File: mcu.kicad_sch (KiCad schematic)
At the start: 41 parts, among them U1 STM32U5G9ZJTxQ, Y1 NX2016SA-16MHZ-EXS00A-CS07826, Y2 NX2012SA-32.768K-STD-MUB-1

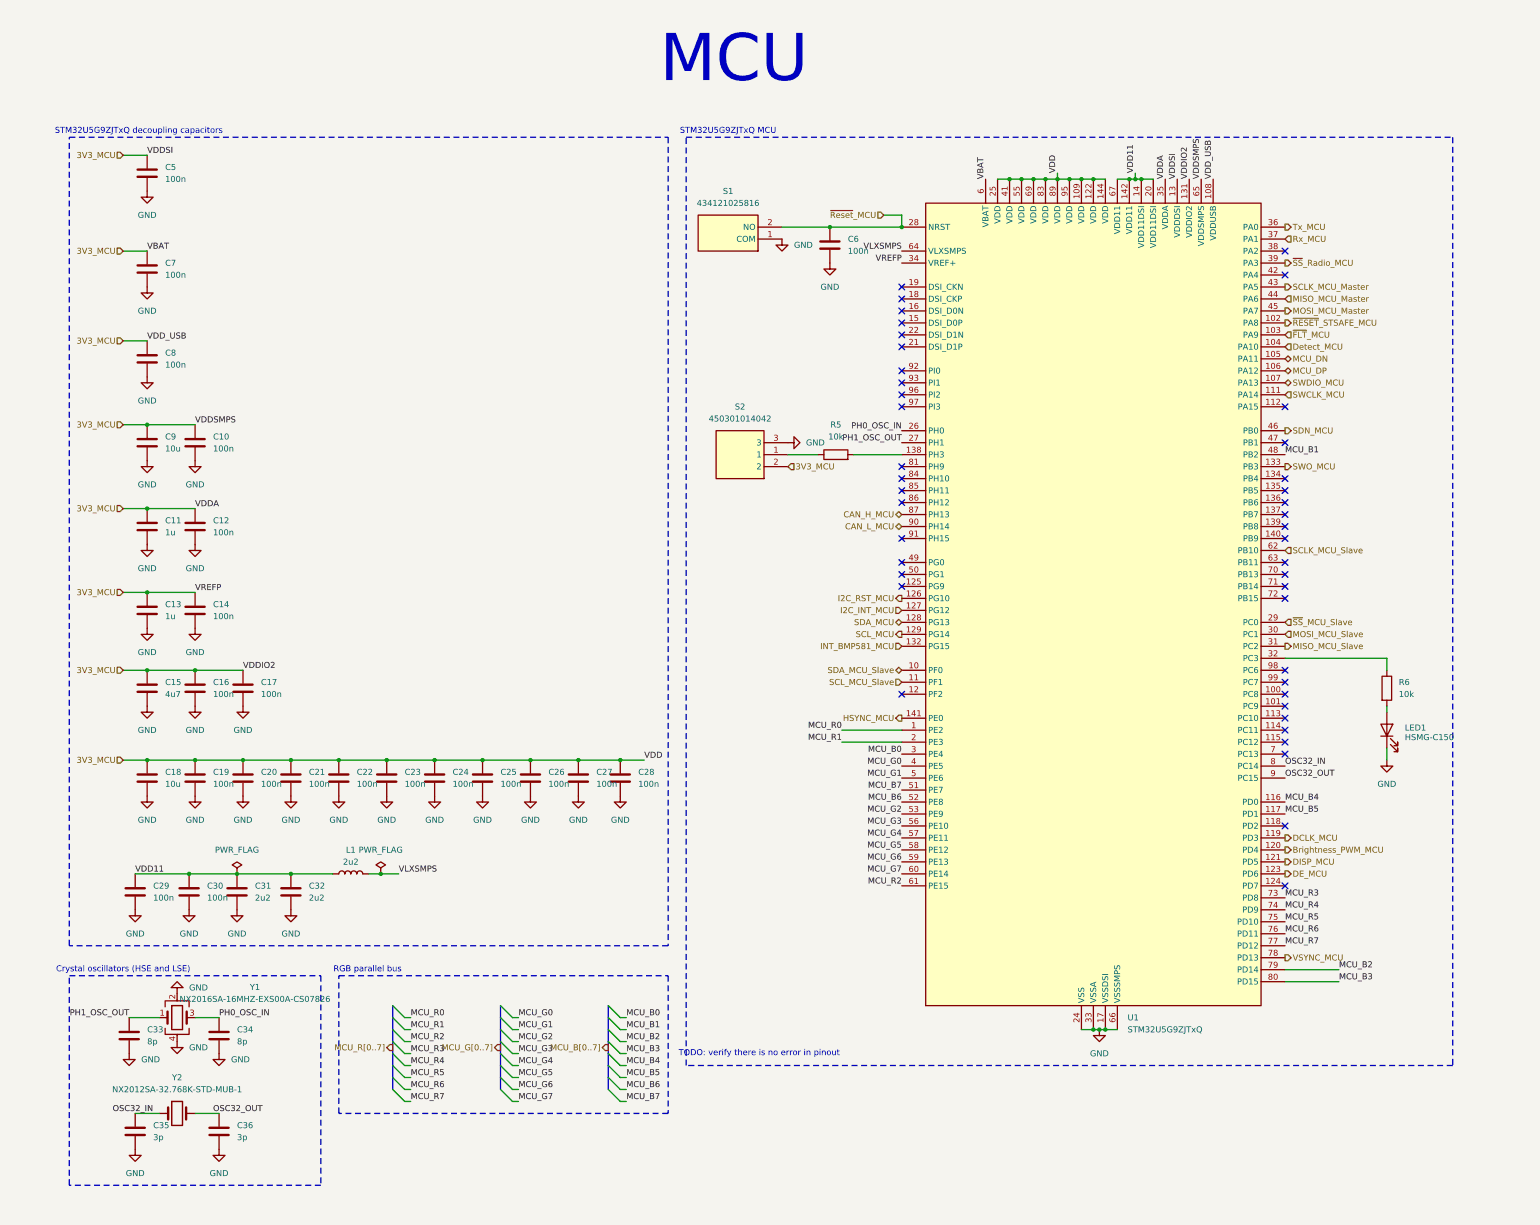
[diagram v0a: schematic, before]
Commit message: Update schematic to Kicad 10
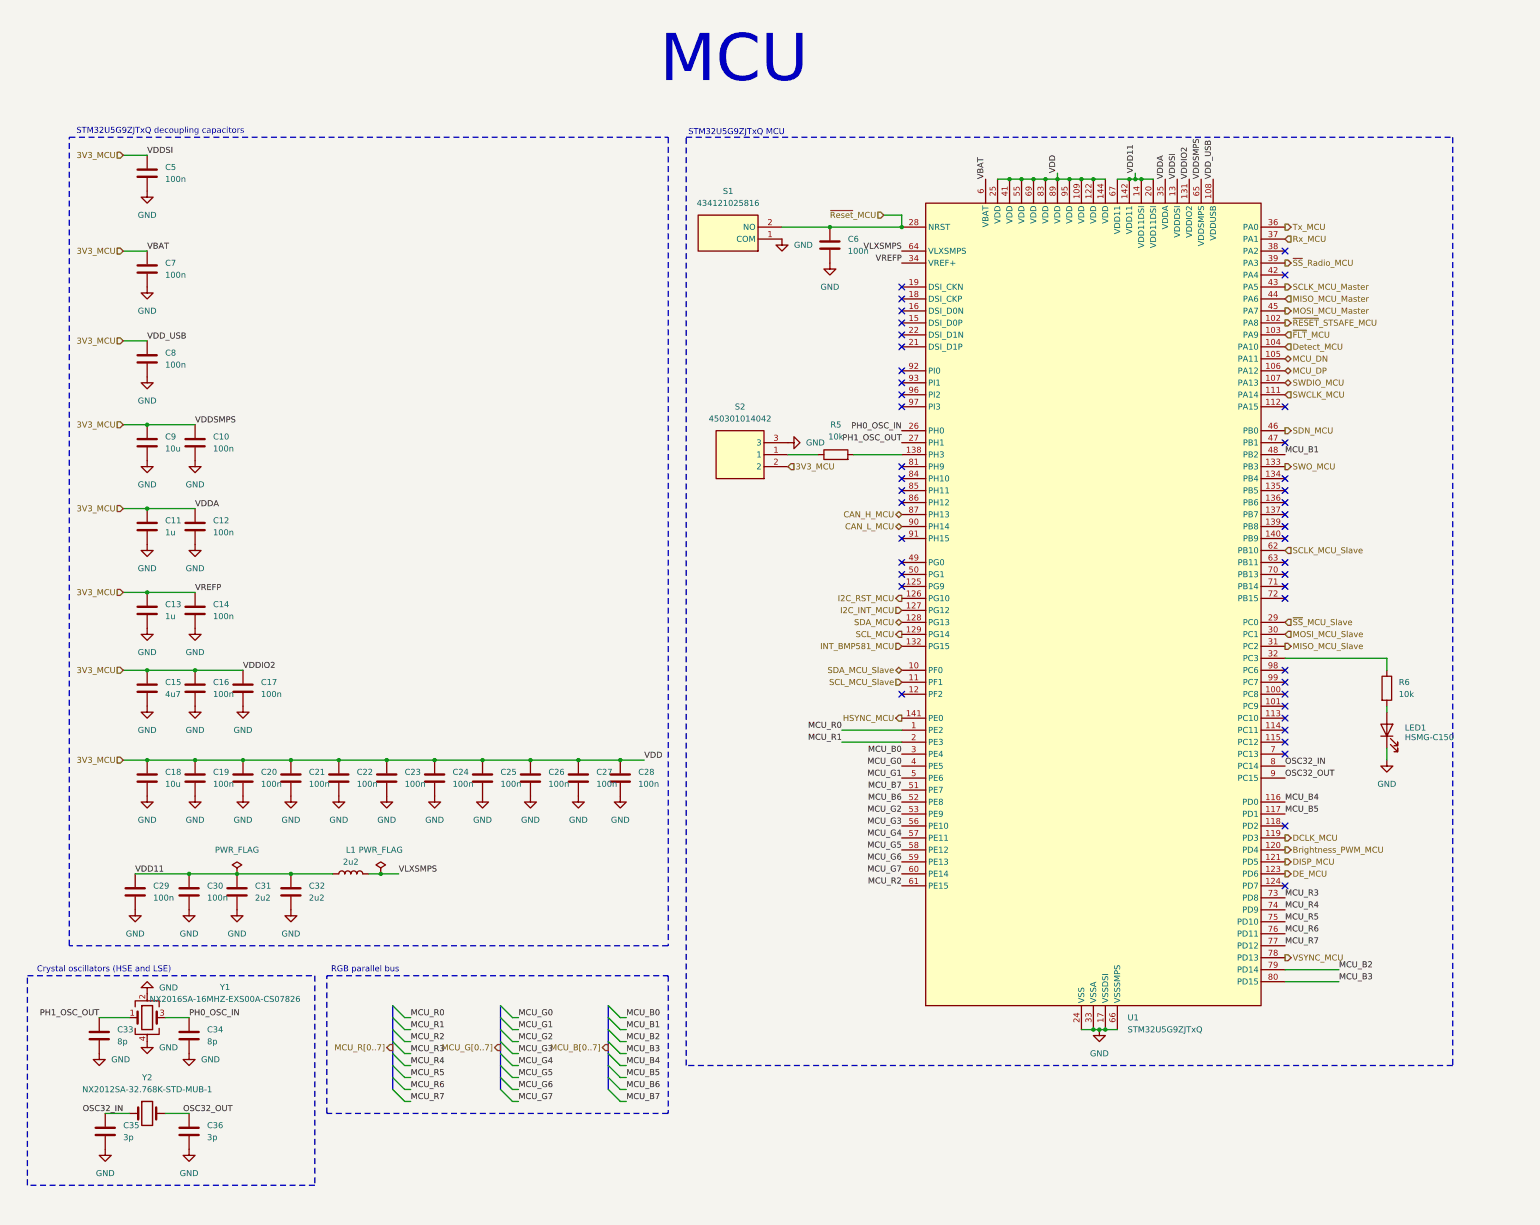
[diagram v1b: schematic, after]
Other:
- note removed: "TODO: verify there is no error in pinout"
- moved on the sheet: C33, C34, C35, C36, Y1, Y2

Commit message: Add tests points with 5015 footprint for practicity
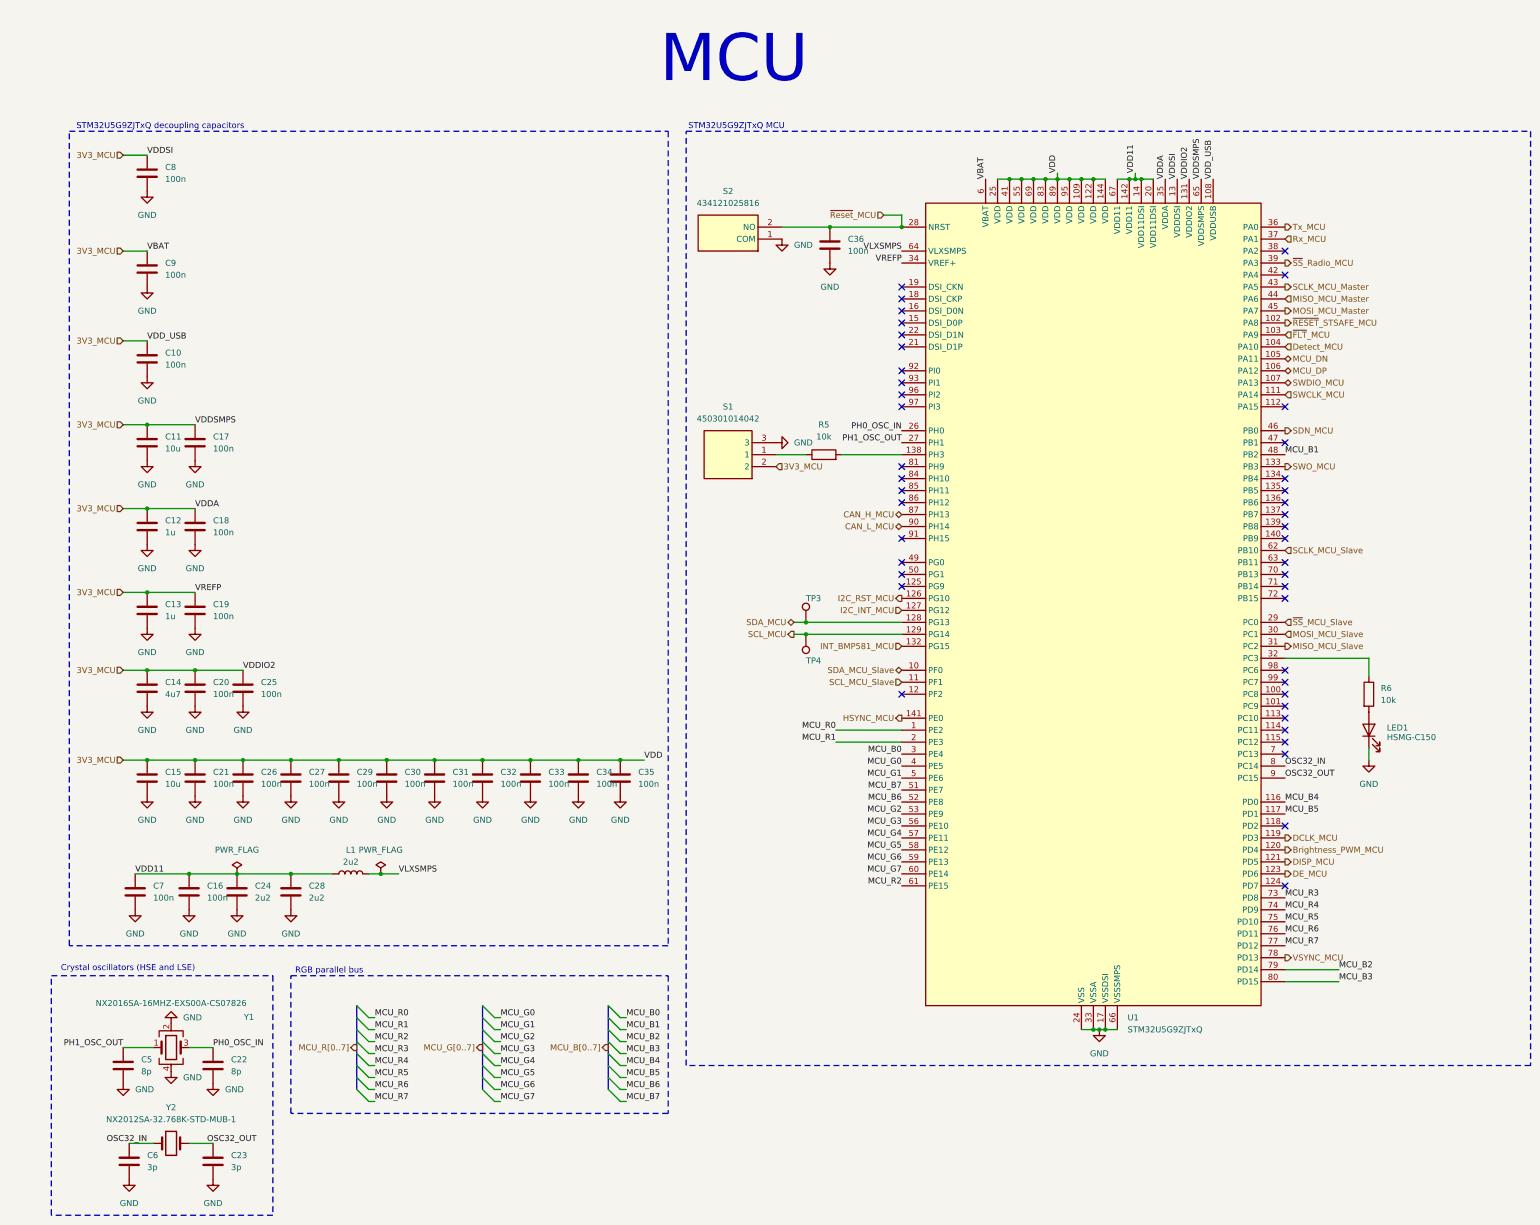
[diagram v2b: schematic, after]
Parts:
- added TP3, TP4: TestPoint, weather-station-poc-fp:5015, symbol Connector:TestPoint
- renumbered C8 to C10, C9 to C11, C11 to C12, C15 to C14, C18 to C15, C30 to C16, C10 to C17, C12 to C18, C14 to C19, C16 to C20, C19 to C21, C34 to C22, C36 to C23, C31 to C24, C17 to C25, C20 to C26, C21 to C27, C32 to C28, C22 to C29, C23 to C30, C24 to C31, C25 to C32, C26 to C33, C27 to C34, C28 to C35, C6 to C36, C33 to C5, C35 to C6, C29 to C7, C5 to C8, C7 to C9, S2 to S1, S1 to S2
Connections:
- net SCL_MCU: now also TP4.1
- net SDA_MCU: now also TP3.1
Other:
- moved on the sheet: C22, C23, C5, C6, LED1, R5, R6, S1, Y1, Y2

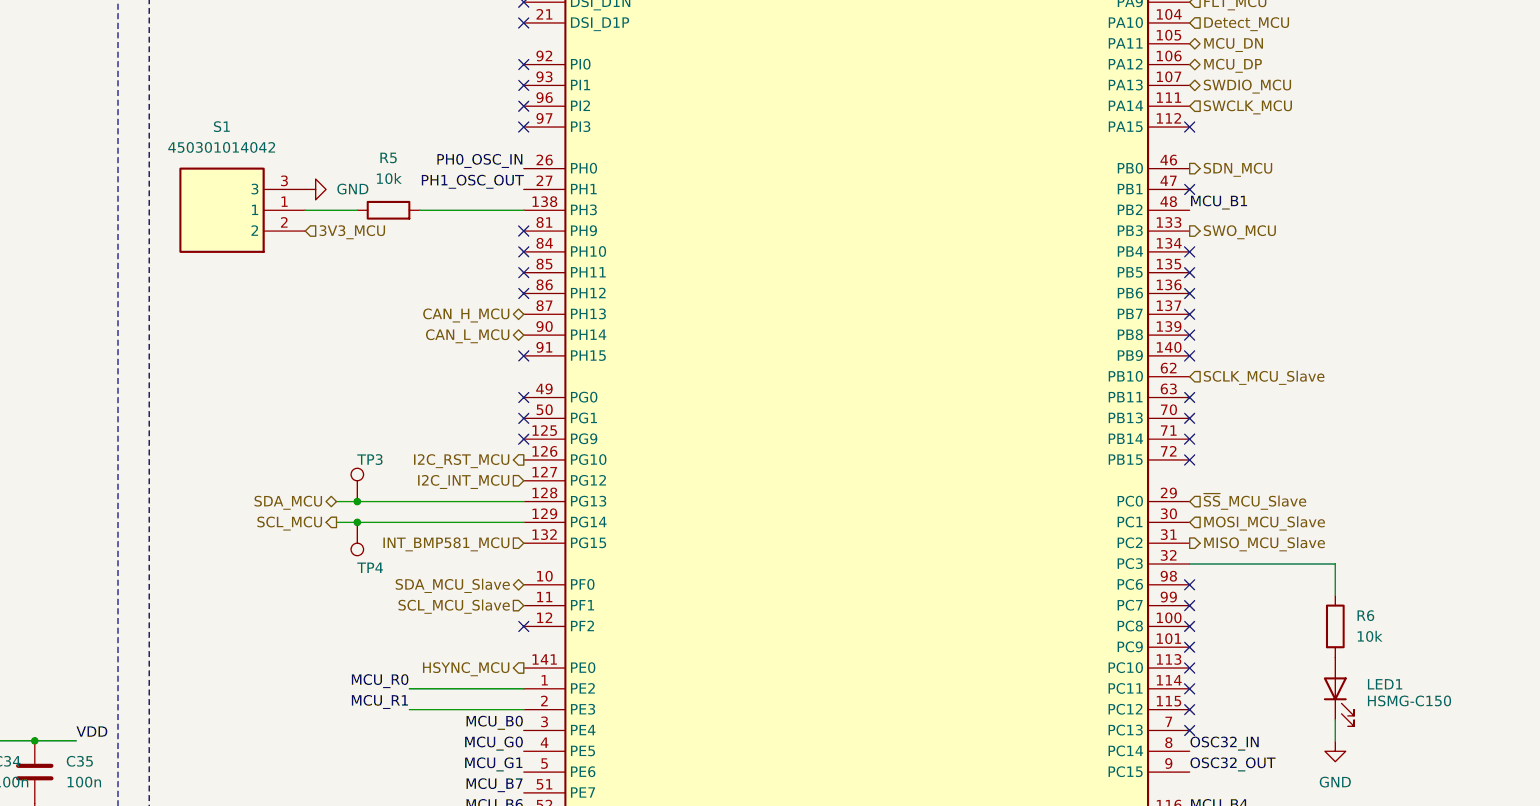
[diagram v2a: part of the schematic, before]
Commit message: Add pull ups resistors for I2C bus and reformat some schematic files
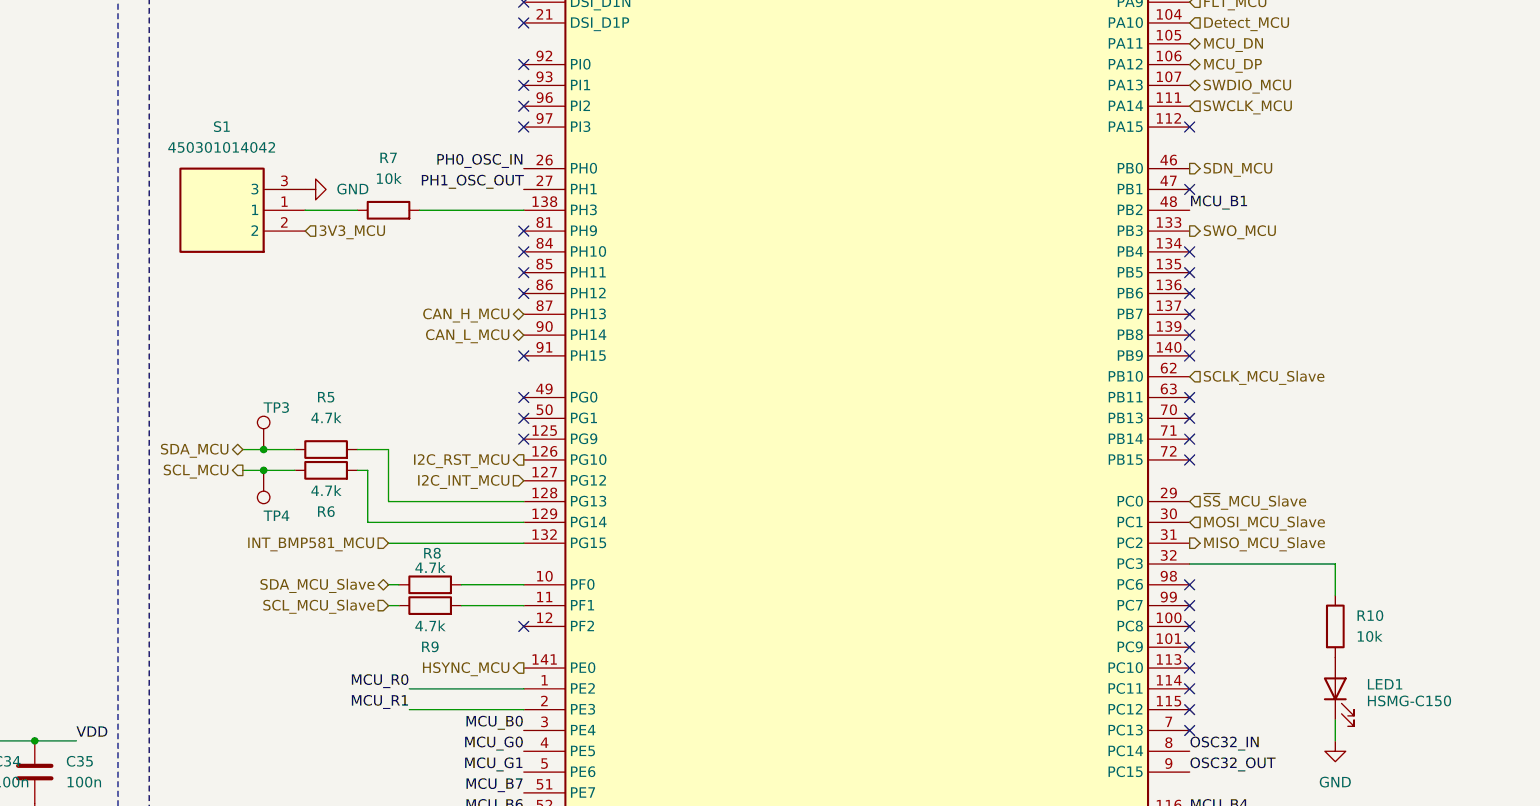
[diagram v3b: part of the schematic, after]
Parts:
- added R5, R6, R8, R9: 4.7k, Resistor_SMD:R_0603_1608Metric_Pad0.98x0.95mm_HandSolder, symbol Device:R
- renumbered R6 to R10, R5 to R7
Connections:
- net SCL_MCU: now also R6.1; no longer U1.129 (PG14)
- net SCL_MCU_Slave: now also R9.1; no longer U1.11 (PF1)
- net SDA_MCU: now also R5.1; no longer U1.128 (PG13)
- net SDA_MCU_Slave: now also R8.1; no longer U1.10 (PF0)
- new net: R8.2, U1.10 (PF0)
- new net: R6.2, U1.129 (PG14)
- new net: R9.2, U1.11 (PF1)
- new net: R5.2, U1.128 (PG13)
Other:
- moved on the sheet: TP3, TP4

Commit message: Complete all references for components
Modifgy Y1 and Y2 capacitors footprint from 0603 to 0402
Modify footprint of SWD connector
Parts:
- C10, C16, C17, C18, C19, C20, C21, C25, C26, C27, C29, C30, C31, C32, C33, C34, C35, C36, C7, C8, C9: Manufacturer_Name (none) -> Wurth Elektronik; Manufacturer_Part_Number (none) -> 885012206020
- C11, C15: Manufacturer_Name (none) -> Murata Electronics; Manufacturer_Part_Number (none) -> GRM188Z71A106KA73D
- C12, C13: Manufacturer_Name (none) -> Wurth Elektronik; Manufacturer_Part_Number (none) -> 885012206026
- C14: Manufacturer_Name (none) -> Murata Electronics; Manufacturer_Part_Number (none) -> GRM188Z71A475KE15J
- C22, C5: footprint Capacitor_SMD:C_0603_1608Metric_Pad1.08x0.95mm_HandSolder -> Capacitor_SMD:C_0402_1005Metric_Pad0.74x0.62mm_HandSolder; Manufacturer_Name (none) -> Walsin; Manufacturer_Part_Number (none) -> 0402N8R0C100CT
- C23, C6: footprint Capacitor_SMD:C_0603_1608Metric_Pad1.08x0.95mm_HandSolder -> Capacitor_SMD:C_0402_1005Metric_Pad0.74x0.62mm_HandSolder; Manufacturer_Name (none) -> KYOCERA AVX; Manufacturer_Part_Number (none) -> 0402ZA3R0BAT2A
- C24, C28: Manufacturer_Name (none) -> Wurth Elektronik; Manufacturer_Part_Number (none) -> 885012206027
- L1: Manufacturer_Name (none) -> Murata Electronics; Manufacturer_Part_Number (none) -> LQM21PN2R2MGHL
- R10, R7: Manufacturer_Name (none) -> Wurth Elektronik; Manufacturer_Part_Number (none) -> 560112116005
- R5, R6, R8, R9: Manufacturer_Name (none) -> Wurth Elektronik; Manufacturer_Part_Number (none) -> 560112116006
- TP3, TP4: Manufacturer_Name (none) -> N/A; Manufacturer_Part_Number (none) -> N/A
- U1: Manufacturer_Name (none) -> STMicroelectronics; Manufacturer_Part_Number (none) -> STM32U5G9ZJT6Q

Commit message: End of BOM
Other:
- moved on the sheet: C22, C23, C5, C6, Y1, Y2

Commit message: Modify reference for 8p and 3p capacitors
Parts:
- C22, C5: Manufacturer_Name Walsin -> YAGEO; Manufacturer_Part_Number 0402N8R0C100CT -> CC0402CRNPO9BN8R2
- C23, C6: Manufacturer_Name KYOCERA AVX -> YAGEO; Manufacturer_Part_Number 0402ZA3R0BAT2A -> CC0402BRNPO9BN3R3
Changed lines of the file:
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@@
 			)
 		)
-		(property "Datasheet" "https://eu.mouser.com/datasheet/3/5926/1/C0GNP0_Dielectric.pdf"
+		(property "Datasheet" "https://www.mouser.fr/datasheet/3/508/1/upy-np0x7r_mv_100-to-630v.pdf"
 			(at 91.44 260.35 0)
 			(hide yes)
@@
 			)
 		)
-		(property "Manufacturer_Name" "KYOCERA AVX"
+		(property "Manufacturer_Name" "YAGEO"
 			(at 91.44 260.35 0)
 			(hide yes)
@@
 			)
 		)
-		(property "Manufacturer_Part_Number" "0402ZA3R0BAT2A"
+		(property "Manufacturer_Part_Number" "CC0402BRNPO9BN3R3 "
 			(at 91.44 260.35 0)
 			(hide yes)
@@
 			)
 		)
-		(property "Datasheet" "https://eu.mouser.com/datasheet/3/317/1/WTC_MLCC_General_Purpose.pdf"
+		(property "Datasheet" "https://www.mouser.fr/datasheet/3/508/1/upy-np0x7r_mv_100-to-630v.pdf"
 			(at 72.39 240.03 0)
 			(hide yes)
@@
 			)
 		)
-		(property "Manufacturer_Name" "Walsin"
+		(property "Manufacturer_Name" "YAGEO"
 			(at 72.39 240.03 0)
 			(hide yes)
@@
 			)
 		)
-		(property "Manufacturer_Part_Number" "0402N8R0C100CT"
+		(property "Manufacturer_Part_Number" "CC0402CRNPO9BN8R2"
 			(at 72.39 240.03 0)
 			(hide yes)
@@
 			)
 		)
-		(property "Datasheet" "https://eu.mouser.com/datasheet/3/317/1/WTC_MLCC_General_Purpose.pdf"
+		(property "Datasheet" "https://www.mouser.fr/datasheet/3/508/1/upy-np0x7r_mv_100-to-630v.pdf"
 			(at 91.44 240.03 0)
 			(hide yes)
@@
 			)
 		)
-		(property "Manufacturer_Name" "Walsin"
+		(property "Manufacturer_Name" "YAGEO"
 			(at 91.44 240.03 0)
 			(hide yes)
@@
 			)
 		)
-		(property "Manufacturer_Part_Number" "0402N8R0C100CT"
+		(property "Manufacturer_Part_Number" "CC0402CRNPO9BN8R2"
 			(at 91.44 240.03 0)
 			(hide yes)
@@
 			)
 		)
-		(property "Datasheet" "https://eu.mouser.com/datasheet/3/5926/1/C0GNP0_Dielectric.pdf"
+		(property "Datasheet" "https://www.mouser.fr/datasheet/3/508/1/upy-np0x7r_mv_100-to-630v.pdf"
 			(at 73.66 260.35 0)
 			(hide yes)
@@
 			)
 		)
-		(property "Manufacturer_Name" "KYOCERA AVX"
+		(property "Manufacturer_Name" "YAGEO"
 			(at 73.66 260.35 0)
 			(hide yes)
@@
 			)
 		)
-		(property "Manufacturer_Part_Number" "0402ZA3R0BAT2A"
+		(property "Manufacturer_Part_Number" "CC0402BRNPO9BN3R3 "
 			(at 73.66 260.35 0)
 			(hide yes)

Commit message: Set I2C address for BMP sensors and document address
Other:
- note added: "Need to estimate bus capacitance to calculate pull ups resistors ?"
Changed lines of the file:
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@@
+		)
+	)
+	(text "Need to estimate bus capacitance \nto calculate pull ups resistors ?"
+		(exclude_from_sim no)
+		(at 194.564 129.54 0)
+		(effects
+			(font
+				(size 1.27 1.27)
+			)
+			(justify left)
 		)
 	)
